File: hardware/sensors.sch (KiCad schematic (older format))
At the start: 17 parts, among them U1 LM358, U2 MCP6001, U3 LAH-100P, U4 LOC110, U5 MCP6001, U6 MCP6001

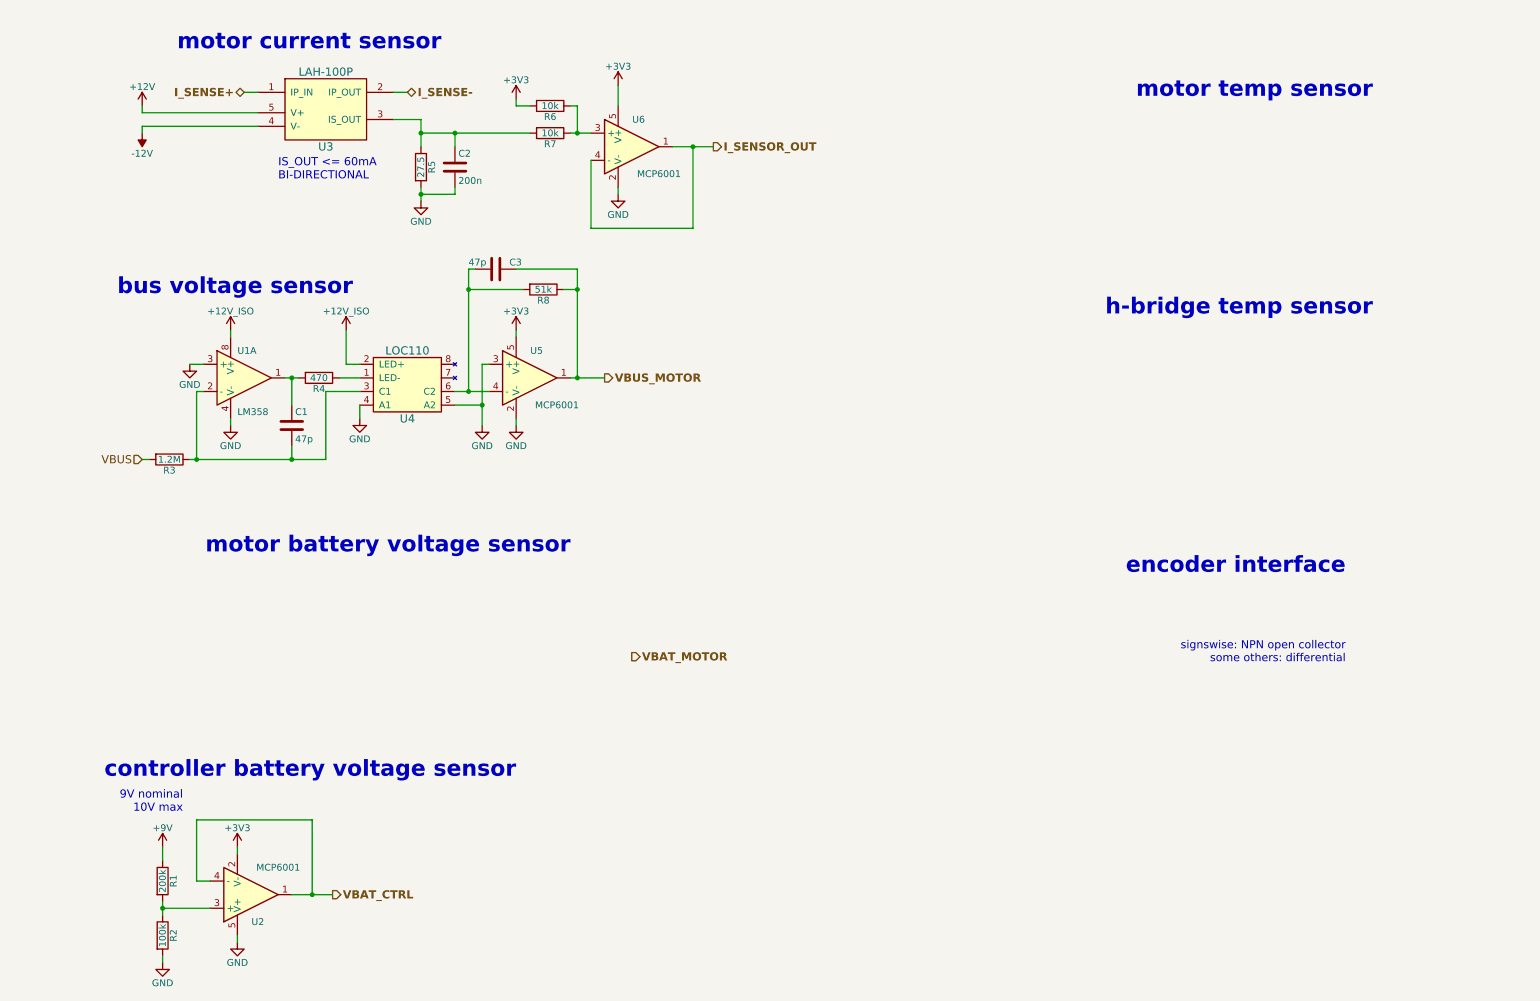
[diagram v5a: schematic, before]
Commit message: Improved current sensor and simplified power supplies
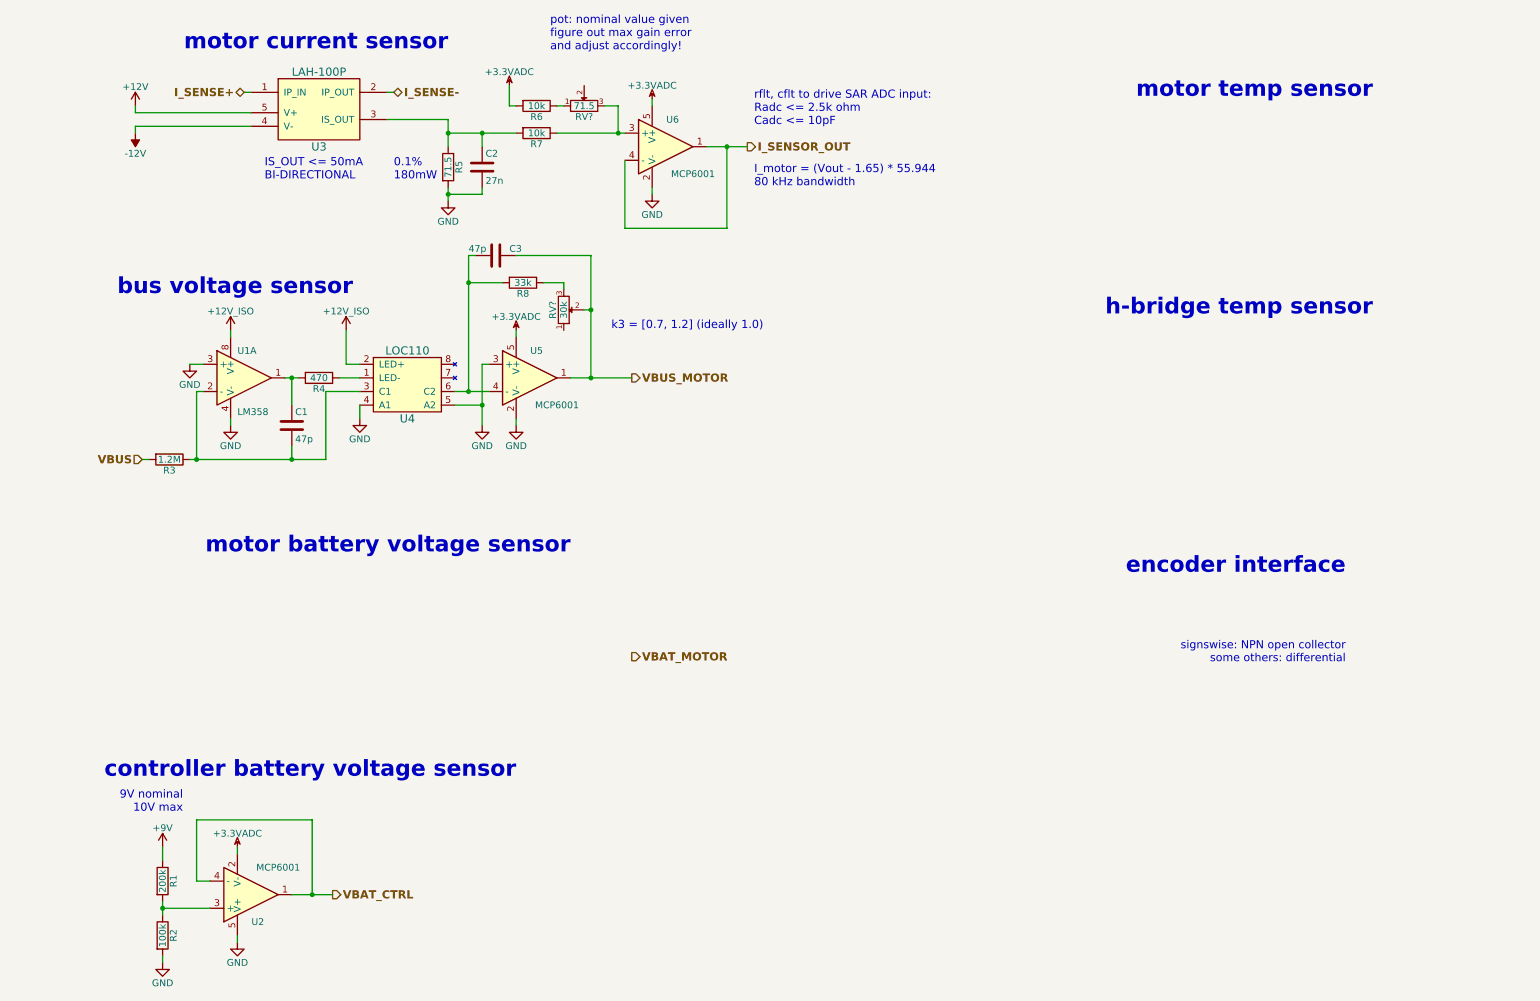
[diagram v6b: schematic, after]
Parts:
- added RV?: 30k, symbol POT
- added RV?: 71.5, symbol POT
- C2: value 200n -> 27n
- R5: value 27.5 -> 71.5
- R8: value 51k -> 33k
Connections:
- net VBUS_MOTOR: now also RV?.2; no longer R8.1
- net at R7.1, U6.3 (+): now also RV?.3; no longer R6.1
- net +3V3 renamed +3.3VADC
- new net: R6.1, RV?.1
- new net: R8.1, RV?.3
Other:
- note added: "0.1%\n180mW"
- note added: "IS_OUT <= 50mA\nBI-DIRECTIONAL"
- note added: "I_motor = (Vout - 1.65) * 55.944\n80 kHz bandwidth"
- note added: "k3 = [0.7, 1.2] (ideally 1.0)"
- note added: "pot: nominal value given\nfigure out max gain error \nand adjust accordingly!"
- note added: "rflt, cflt to drive SAR ADC input:\nRadc <= 2.5k ohm\nCadc <= 10pF"
- note removed: "IS_OUT <= 60mA\nBI-DIRECTIONAL"
- moved on the sheet: C2, C3, R5, R6, R7, R8, U3, U6

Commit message: Chose components and simulated LT3471
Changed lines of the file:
@@
 	2650 1250 3100 1250
 Wire Wire Line
-	3100 1250 3100 1350
+	3100 1250 3100 1450
 Wire Wire Line
-	3100 1350 3100 1450
-Wire Wire Line
-	3100 1750 3100 1800
-Wire Wire Line
-	3100 1800 3100 1850
+	3100 1750 3100 1850
 Wire Wire Line
 	3100 1800 3350 1800
@@
 	3350 1450 3350 1350
 Wire Wire Line
-	3100 1350 3350 1350
-Wire Wire Line
-	3350 1350 3600 1350
+	3100 1350 3600 1350
 Connection ~ 3100 1350
 Wire Wire Line
@@
 	5150 2050 5150 1450
 Wire Wire Line
-	5000 1450 5150 1450
-Wire Wire Line
-	5150 1450 5300 1450
+	5000 1450 5300 1450
 Connection ~ 5150 1450
 Wire Wire Line
@@
 	4350 1150 4350 1350
 Wire Wire Line
-	3900 1350 4350 1350
-Wire Wire Line
-	4350 1350 4400 1350
+	3900 1350 4400 1350
 Connection ~ 4350 1350
 Connection ~ 3350 1350
@@
 	1000 7400 1000 7450
 Wire Wire Line
-	1000 7000 1000 7050
-Wire Wire Line
-	1000 7050 1000 7100
+	1000 7000 1000 7100
 Wire Wire Line
 	1000 6700 1000 6600
@@
 	1550 7250 1550 7300
 Wire Wire Line
-	1950 6950 2100 6950
-Wire Wire Line
-	2100 6950 2250 6950
+	1950 6950 2250 6950
 Wire Wire Line
 	2100 6950 2100 6400
@@
 	2300 3150 2450 3150
 Wire Wire Line
-	1900 3150 1950 3150
-Wire Wire Line
-	1950 3150 2000 3150
+	1900 3150 2000 3150
 Wire Wire Line
 	1500 3450 1500 3500
@@
 	2450 3250 2200 3250
 Wire Wire Line
-	2200 3250 2200 3750
+	2200 3750 2200 3250
 Wire Wire Line
-	2200 3750 1950 3750
-Wire Wire Line
-	1950 3750 1250 3750
-Wire Wire Line
-	1250 3750 1200 3750
+	1200 3750 2200 3750
 Wire Wire Line
 	1250 3750 1250 3250
@@
 Connection ~ 1950 3150
 Wire Wire Line
-	3150 3250 3250 3250
-Wire Wire Line
-	3250 3250 3400 3250
+	3150 3250 3400 3250
 Wire Wire Line
 	3600 3450 3600 3500
@@
 	3400 3050 3350 3050
 Wire Wire Line
-	3350 3050 3350 3350
-Wire Wire Line
-	3350 3350 3350 3500
+	3350 3050 3350 3500
 Wire Wire Line
 	3350 3350 3150 3350
 Wire Wire Line
-	4000 3150 4150 3150
-Wire Wire Line
-	4150 3150 4450 3150
+	4000 3150 4450 3150
 Wire Wire Line
 	3500 2450 3250 2450
 Wire Wire Line
-	3250 2250 3250 2450
-Wire Wire Line
-	3250 2450 3250 3250
+	3250 2250 3250 3250
 Connection ~ 3250 3250
 Wire Wire Line
@@
 	4100 2650 4150 2650
 Wire Wire Line
-	4150 2250 4150 2650
-Wire Wire Line
-	4150 2650 4150 3150
+	4150 2250 4150 3150
 Connection ~ 4150 3150
 Connection ~ 4150 2650

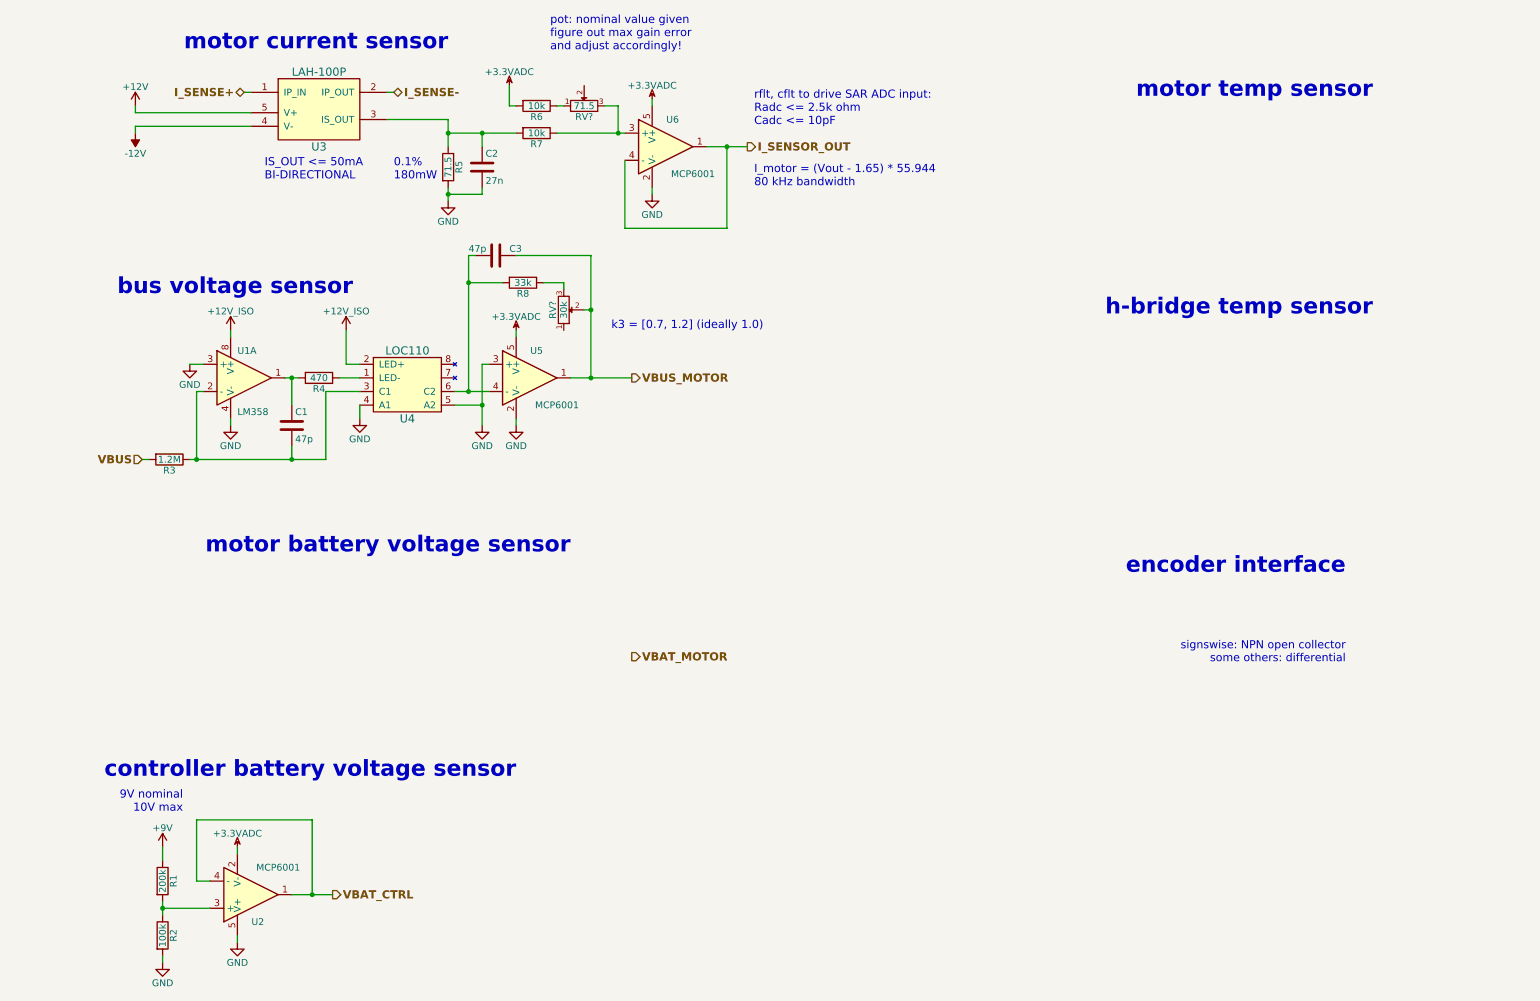
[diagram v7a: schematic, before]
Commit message: Finish MCU HW draft 1; adjust sensors for 3v ref
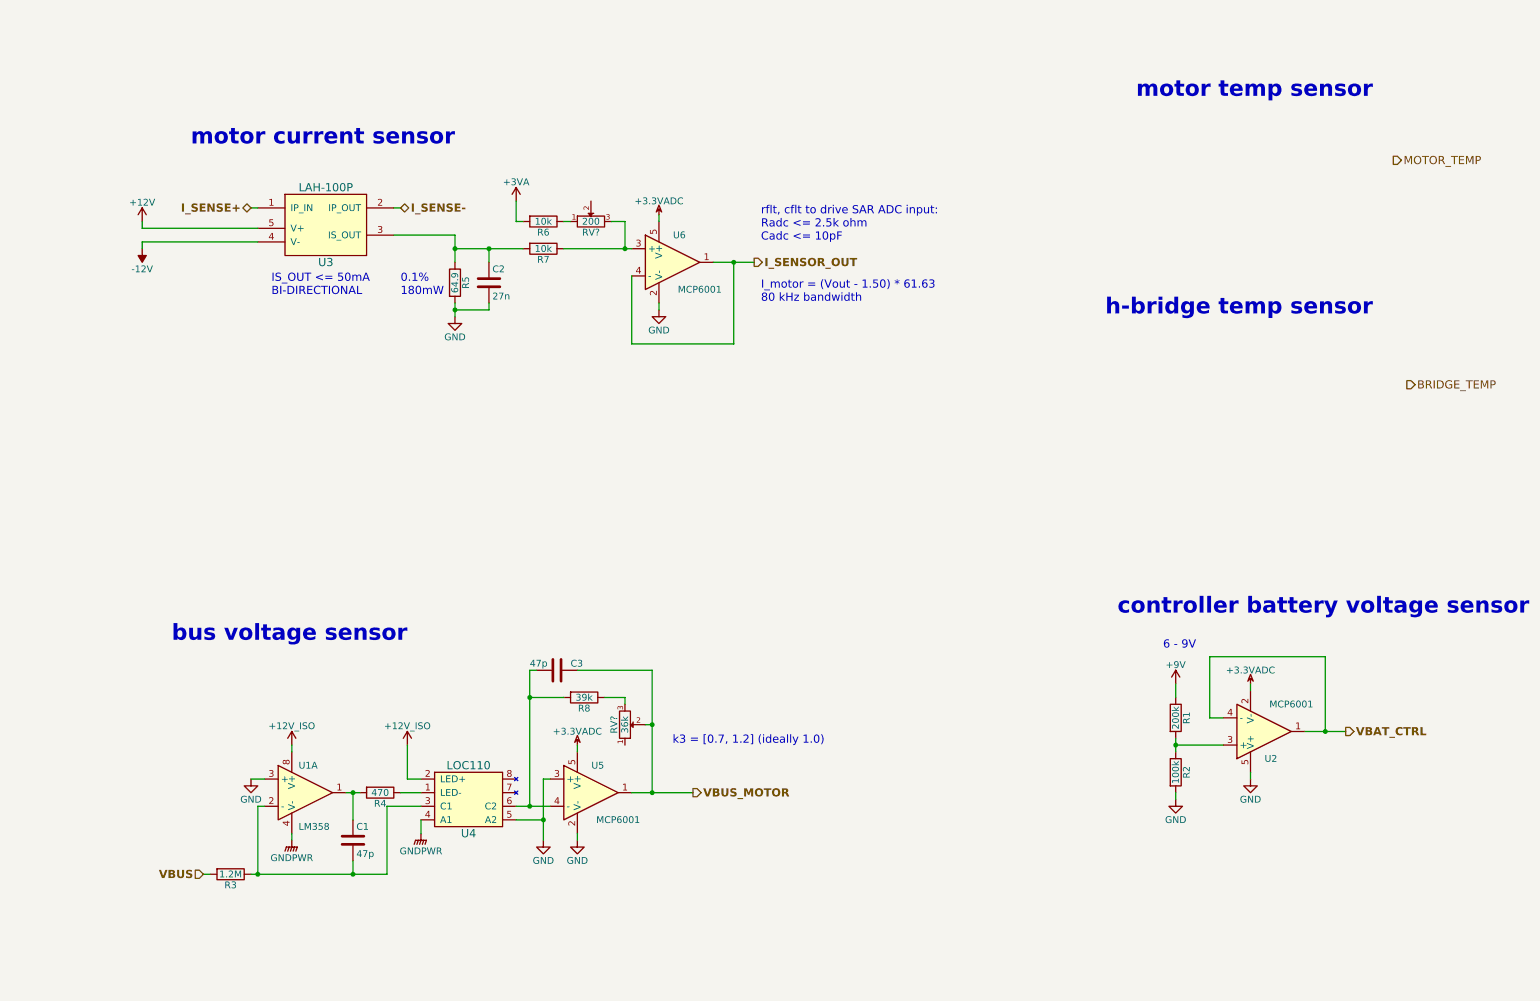
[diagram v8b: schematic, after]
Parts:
- R5: value 71.5 -> 64.9
- R8: value 33k -> 39k
- RV?: value 30k -> 36k
- RV?: value 71.5 -> 200
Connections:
- net +3.3VADC: no longer R6.2
- net GND: no longer U1.4 (V-), U4.4 (A1)
- new net +3V3: R6.2
- new net GNDPWR: U1.4 (V-), U4.4 (A1)
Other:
- note added: "6 - 9V"
- note added: "I_motor = (Vout - 1.50) * 61.63\n80 kHz bandwidth"
- note removed: "9V nominal\n10V max"
- note removed: "I_motor = (Vout - 1.65) * 55.944\n80 kHz bandwidth"
- note removed: "encoder interface"
- note removed: "motor battery voltage sensor"
- note removed: "pot: nominal value given\nfigure out max gain error \nand adjust accordingly!"
- note removed: "signswise: NPN open collector\nsome others: differential"
- moved on the sheet: C1, C2, C3, R1, R2, R3, R4, R5, R6, R7, R8, RV?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
